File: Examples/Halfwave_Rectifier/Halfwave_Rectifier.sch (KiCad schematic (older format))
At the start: 3 parts

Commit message: Modified Example
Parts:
- R1: symbol R -> R-RESCUE-Halfwave_Rectifier
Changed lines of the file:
@@
 EESchema Schematic File Version 2
+LIBS:eSim_Analog
+LIBS:eSim_Devices
+LIBS:eSim_Digital
+LIBS:eSim_Hybrid
+LIBS:eSim_Miscellaneous
+LIBS:eSim_Sources
 LIBS:eSim_Subckt
-LIBS:eSim_Sources
-LIBS:eSim_Hybrid
-LIBS:eSim_Digital
-LIBS:eSim_Devices
-LIBS:eSim_Analog
-LIBS:eSim_Miscellaneous
 LIBS:eSim_User
+LIBS:Halfwave_Rectifier-rescue
 LIBS:power
 LIBS:device
@@
 $EndComp
 $Comp
-L R R1
+L R-RESCUE-Halfwave_Rectifier R1
 U 1 1 5593CC2C
 P 6300 3350

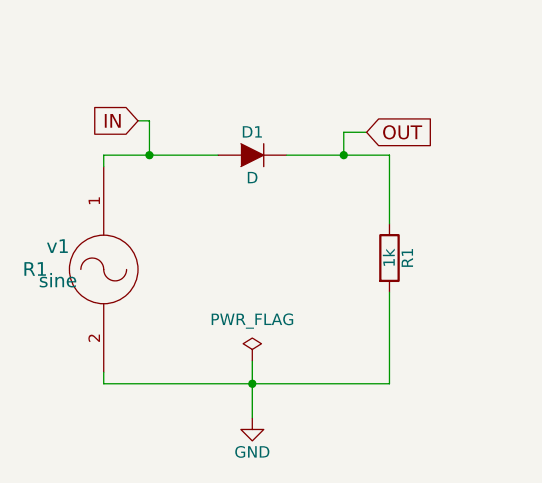
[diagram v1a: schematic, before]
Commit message: Remove unwanted example
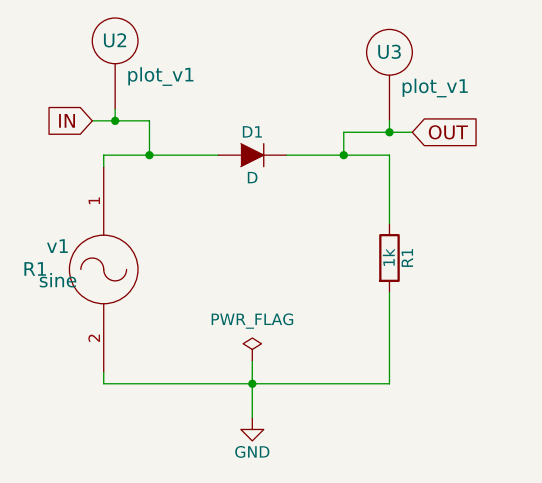
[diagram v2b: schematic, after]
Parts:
- added U2, U3: plot_v1, symbol plot_v1
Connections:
- net IN: now also U2.~
- net OUT: now also U3.~
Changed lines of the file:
@@
 LIBS:eSim_Hybrid
 LIBS:eSim_Miscellaneous
+LIBS:eSim_Plot
+LIBS:eSim_Power
 LIBS:eSim_Sources
 LIBS:eSim_Subckt
@@
 	1    0    0    -1
 $EndComp
+$Comp
+L PWR_FLAG #FLG02
+U 1 1 5593CD49
+P 5700 3800
+F 0 "#FLG02" H 5700 3895 50  0001 C CNN
+F 1 "PWR_FLAG" H 5700 3980 50  0000 C CNN
+F 2 "" H 5700 3800 60  0000 C CNN
+F 3 "" H 5700 3800 60  0000 C CNN
+	1    5700 3800
+	1    0    0    -1
+$EndComp
+Text GLabel 5000 2750 0    60   Input ~ 0
+IN
+Text GLabel 6400 2800 2    60   Input ~ 0
+OUT
+$Comp
+L plot_v1 U2
+U 1 1 56D86A9A
+P 5100 2900
+F 0 "U2" H 5100 3400 60  0000 C CNN
+F 1 "plot_v1" H 5300 3250 60  0000 C CNN
+F 2 "" H 5100 2900 60  0000 C CNN
+F 3 "" H 5100 2900 60  0000 C CNN
+	1    5100 2900
+	1    0    0    -1
+$EndComp
+$Comp
+L plot_v1 U3
+U 1 1 56D86ADF
+P 6300 2950
+F 0 "U3" H 6300 3450 60  0000 C CNN
+F 1 "plot_v1" H 6500 3300 60  0000 C CNN
+F 2 "" H 6300 2950 60  0000 C CNN
+F 3 "" H 6300 2950 60  0000 C CNN
+	1    6300 2950
+	1    0    0    -1
+$EndComp
 Wire Wire Line
 	5050 2950 5050 2900
@@
 	5700 3800 5700 4050
 Connection ~ 5700 3900
-$Comp
-L PWR_FLAG #FLG02
-U 1 1 5593CD49
-P 5700 3800
-F 0 "#FLG02" H 5700 3895 50  0001 C CNN
-F 1 "PWR_FLAG" H 5700 3980 50  0000 C CNN
-F 2 "" H 5700 3800 60  0000 C CNN
-F 3 "" H 5700 3800 60  0000 C CNN
-	1    5700 3800
-	1    0    0    -1
-$EndComp
-Text GLabel 5200 2750 0    60   Input ~ 0
-IN
-Text GLabel 6200 2800 2    60   Input ~ 0
-OUT
 Wire Wire Line
-	5200 2750 5250 2750
+	5000 2750 5250 2750
 Wire Wire Line
 	5250 2750 5250 2900
 Connection ~ 5250 2900
 Wire Wire Line
-	6200 2800 6100 2800
+	6100 2800 6400 2800
 Wire Wire Line
 	6100 2800 6100 2900
 Connection ~ 6100 2900
+Wire Wire Line
+	5100 2700 5100 2750
+Connection ~ 5100 2750
+Wire Wire Line
+	6300 2750 6300 2800
+Connection ~ 6300 2800
 $EndSCHEMATC

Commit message: common code for Win and Linux, merged py2 changes
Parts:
- D1: symbol D -> D-RESCUE-Halfwave_Rectifier
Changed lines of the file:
@@
 EESchema Schematic File Version 2
+LIBS:Halfwave_Rectifier-rescue
 LIBS:eSim_Analog
 LIBS:eSim_Devices
@@
 LIBS:eSim_Subckt
 LIBS:eSim_User
-LIBS:Halfwave_Rectifier-rescue
 LIBS:power
 LIBS:device
@@
 LIBS:contrib
 LIBS:valves
+LIBS:eSim_PSpice
 LIBS:Halfwave_Rectifier-cache
 EELAYER 25 0
@@
 $EndDescr
 $Comp
-L D D1
+L D-RESCUE-Halfwave_Rectifier D1
 U 1 1 5593CBB8
 P 5700 2900
